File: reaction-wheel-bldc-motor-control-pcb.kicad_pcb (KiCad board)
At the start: 2 copper layers, 50 parts, among them J1 Conn_01x04_Pin, J2 Conn_01x04_Pin, J3 Conn_01x03_Pin, J4 USB_C_Receptacle_USB2.0_16P, J5 Conn_01x04_Pin, J6 Conn_01x06_Pin, SW1 SW_SPST, U1 USBLC6-2SC6, U2 STM32G431CBUx, U4 DRV8311H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

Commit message: started with pcb routing
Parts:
- removed C13: 1u, Capacitor_SMD:C_0603_1608Metric
- removed C6: 0.1u, Capacitor_SMD:C_0402_1005Metric
- moved C21 93.6 mm to (109.9, 127.8)
- moved R1 70.4 mm to (145.2, 123.3)
- moved R2 70.4 mm to (145.2, 127.3)
- moved U1 70.4 mm to (141.2, 125.8)
- moved L1 69.3 mm to (112.5, 128.1), turned to 0 degrees
- moved J4 68.6 mm to (153.5, 125.5)
- moved U6 65.7 mm to (112.0, 124.7), turned to 90 degrees
- moved H3 63.2 mm to (154.0, 143.1)
- moved C20 62.9 mm to (111.5, 121.8), turned to 0 degrees
- moved R6 62.8 mm to (114.8, 124.1), turned to -90 degrees
- moved H2 61.9 mm to (107.3, 143.2)
- moved R5 61.4 mm to (116.5, 124.1), turned to 90 degrees
- moved MT1 60.9 mm to (118.7, 113.1), turned to 180 degrees
- moved D2 59.9 mm to (113.7, 137.8), turned to 0 degrees
- moved D1 57.1 mm to (113.7, 134.0), turned to 0 degrees
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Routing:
- net +3.3V: track 20.7 -> 140.8 mm, vias 0 -> 2
- net +5V: track 0.00 -> 54.8 mm, vias 0 -> 2
- net /SWDCLK: track 0.00 -> 24.8 mm
- net /SWDIO: track 0.00 -> 23.9 mm
- net /I2C1_SDA: track 0.00 -> 23.3 mm
- net /I2C1_SCL: track 0.00 -> 21.8 mm
- net VBAT: track 2.99 -> 23.0 mm
- net /FAULT: track 2.70 -> 20.7 mm
- net /SLEEP: track 1.66 -> 17.6 mm
- net /SPI1_MOSI: track 0.00 -> 15.0 mm
- net /USBR_D+: track 4.91 -> 18.0 mm
- net /SPI1_MISO: track 0.00 -> 12.8 mm
- net /PA9: track 0.00 -> 12.2 mm
- net /PA10: track 0.00 -> 12.1 mm
- net /PA8: track 0.00 -> 12.0 mm
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- added copper zone on B.Cu, net GND
- added copper zone on F.Cu, net GND
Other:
- board outline added: 52.6 x 38.7 mm

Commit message: routing almost finished
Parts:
- C1, C16, C17, C21: footprint Capacitor_SMD:C_0603_1608Metric -> Capacitor_SMD:C_0805_2012Metric
- C10, C11, C12, C14, C15, C18, C19, C2, C20, C3, C4, C5, C7, C8, C9: footprint Capacitor_SMD:C_0402_1005Metric -> Capacitor_SMD:C_0805_2012Metric
- moved H1 70.6 mm to (163.1, 67.1)
- moved H2 64.2 mm to (162.8, 111.0)
- moved D2 55.0 mm to (125.7, 84.0), turned to 90 degrees
- moved H4 54.9 mm to (120.1, 67.2)
- moved D1 50.6 mm to (121.8, 84.0), turned to 90 degrees
- moved C4 49.8 mm to (134.5, 86.3), turned to 180 degrees
- moved C11 49.2 mm to (148.5, 86.5), turned to 90 degrees
- moved H3 46.6 mm to (120.3, 110.9)
- moved C1 46.6 mm to (132.9, 89.2), turned to 90 degrees
- moved C8 45.7 mm to (134.5, 84.1), turned to 180 degrees
- moved C9 45.4 mm to (146.3, 86.5), turned to 90 degrees
- moved J3 44.3 mm to (151.6, 100.4), turned to 180 degrees
- moved C5 42.4 mm to (133.7, 98.7), turned to 0 degrees
- moved FB1 41.9 mm to (144.2, 97.1)
- moved SW1 41.8 mm to (131.0, 103.0)
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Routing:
- net VBAT: track 23.0 -> 85.5 mm
- net /PA1: track 0.00 -> 39.0 mm, vias 0 -> 2
- net /PA0: track 0.00 -> 38.4 mm, vias 0 -> 2
- net /PB0: track 0.00 -> 36.0 mm
- net GND: track 0.50 -> 16.7 mm, vias 0 -> 4
- net +3.3V: track 140.8 -> 128.7 mm
- net /CAN_H: track 19.1 -> 8.16 mm
- net /USBR_D+: track 18.0 -> 7.13 mm
- net /USBR_D-: track 17.3 -> 7.34 mm
- net +5V: track 54.8 -> 46.4 mm
- net /MOTOR_C: track 1.20 -> 9.16 mm
- net /FAULT: track 20.7 -> 28.4 mm
- net /PA8: track 12.0 -> 19.5 mm
- net /PA9: track 12.2 -> 19.5 mm
- net /PA10: track 12.1 -> 19.4 mm
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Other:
- board size 52.6 x 38.7 mm -> 48.6 x 49.5 mm

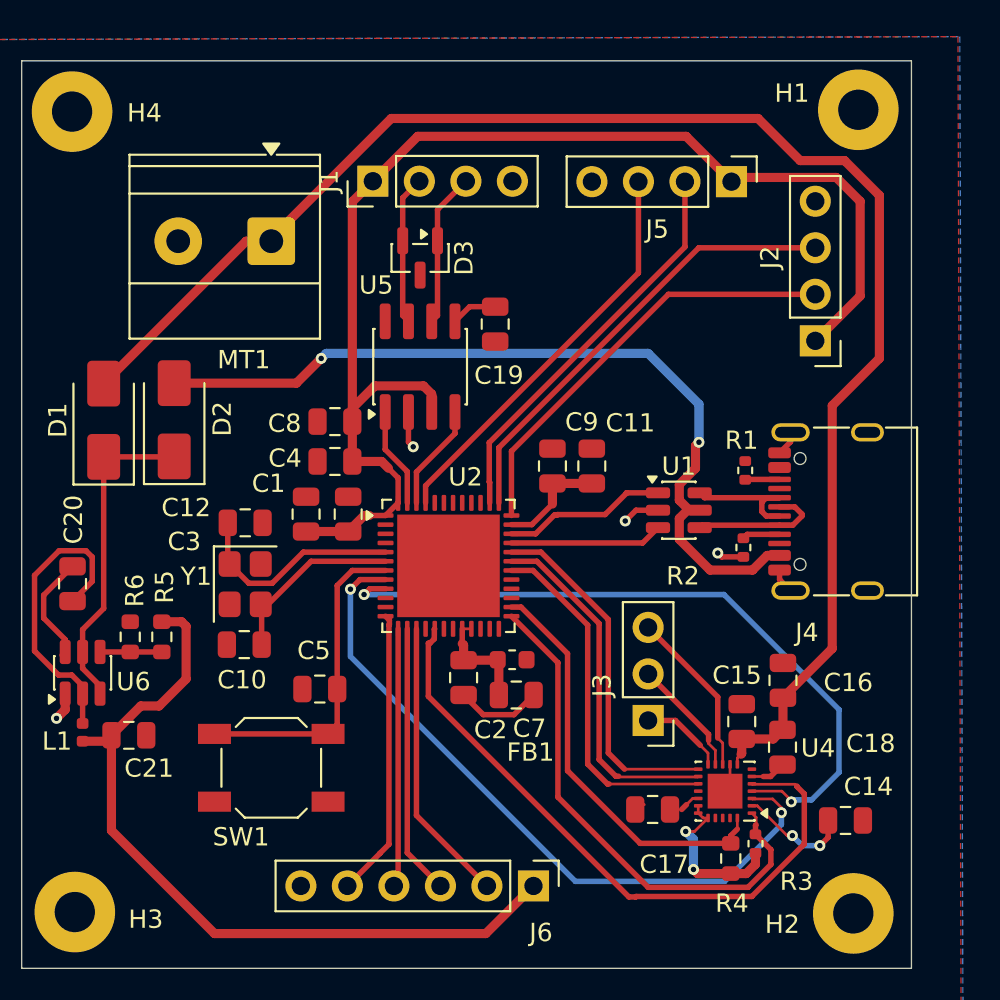
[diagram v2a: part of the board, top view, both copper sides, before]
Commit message: fixed unrouted connections
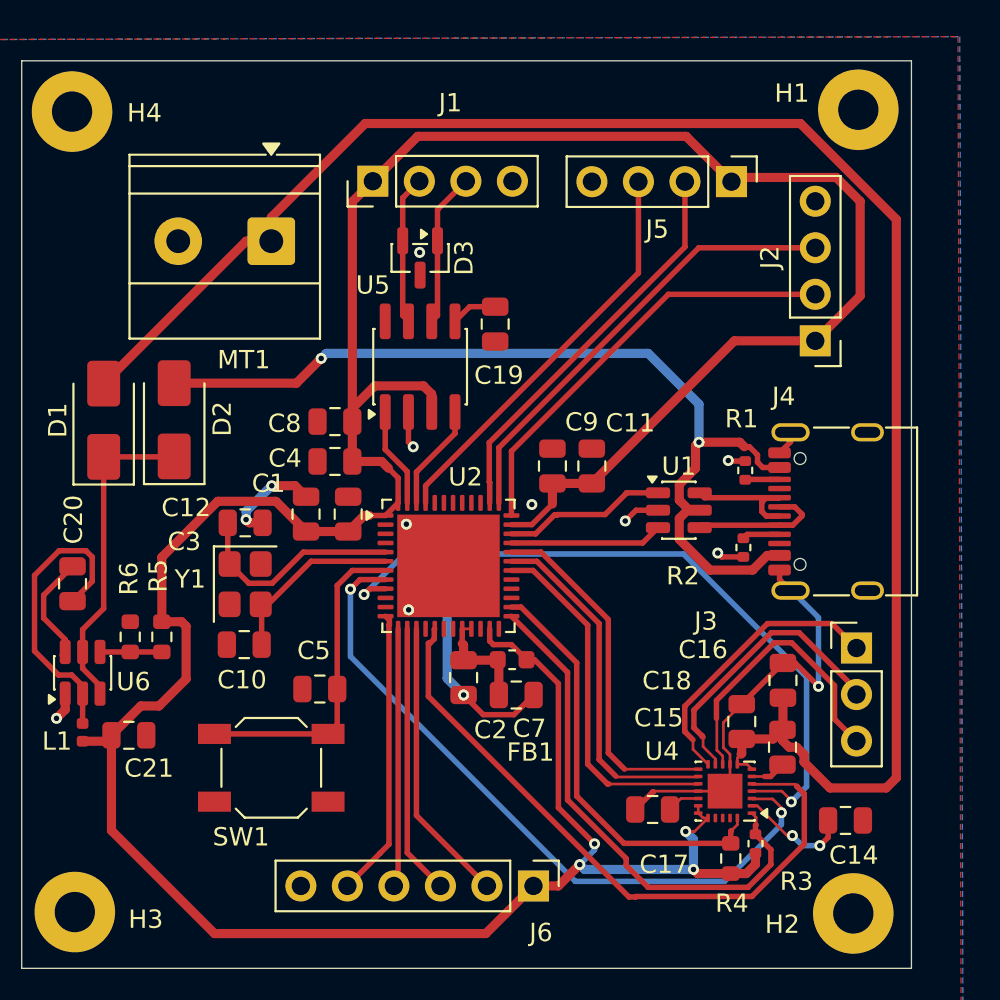
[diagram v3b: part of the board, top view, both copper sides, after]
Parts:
- moved J3 12.0 mm to (162.9, 96.5), turned to 0 degrees
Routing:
- net +3.3V: track 128.7 -> 183.2 mm, vias 2 -> 4
- net GND: track 16.7 -> 51.4 mm, vias 4 -> 13
- net VBAT: track 85.5 -> 97.5 mm
- net /MOTOR_A: track 4.62 -> 15.5 mm
- net /MOTOR_B: track 6.46 -> 15.7 mm
- net /MOTOR_C: track 9.16 -> 16.0 mm
- net +5V: track 46.4 -> 51.6 mm
- net Net-(U4-AVDD): track 1.15 -> 1.79 mm
- net /SLEEP: track 22.6 -> 23.1 mm
